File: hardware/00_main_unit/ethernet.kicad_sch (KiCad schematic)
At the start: 25 parts, among them IC5 LAN8742A, J11 LMJ1998824110DL1T39J, Y2 ABM7-25.000MHZ-D2Y-T

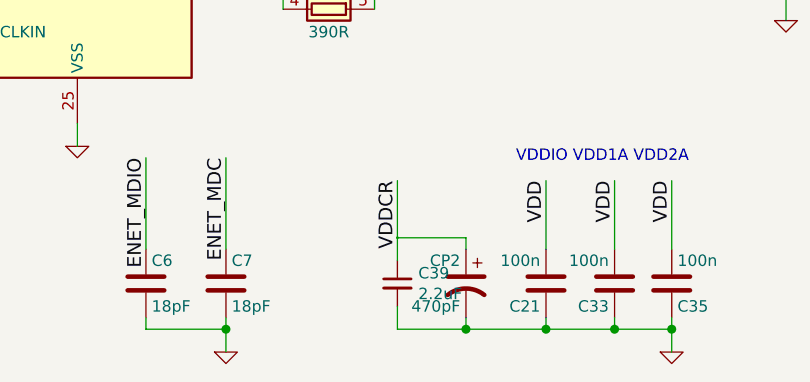
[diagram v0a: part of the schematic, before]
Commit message: Fixes after wrong merge
Signed-off-by: Jacek <matuszewski.kartech@gmail.com>
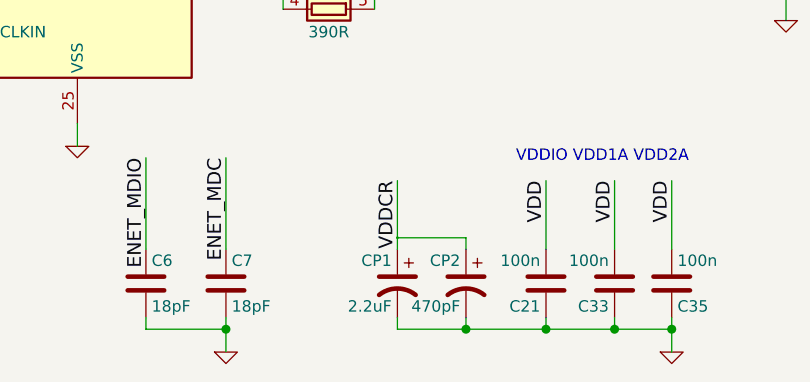
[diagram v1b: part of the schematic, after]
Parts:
- removed C39: 2.2uF, Capacitor_SMD:C_0603_1608Metric, symbol Device:C_Small
- added CP1: 2.2uF, Capacitor_SMD:C_0603_1608Metric, symbol Device:CP1
- C21, C33, C35, C36, C37: TME C0603C104K3RAC -> (none)
- C4, C5, C6, C7: TME 0603N180G500CT -> (none)
- C9: TME CL10A106MQ8NNNC -> (none)
- R1: TME WF06P-33R-5% -> (none)
- R38: TME SMD0603-12.1K-1% -> (none)
- R45, R46, R47, R48: TME SMD0603-49R9-1% -> (none)
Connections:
- net GND: now also CP1.2
- net VDDCR: now also CP1.1
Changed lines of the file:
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@@
     (stroke (width 0) (type solid) (color 0 0 0 0))
   )
-  (wire (pts (xy 168.91 129.54) (xy 168.91 132.08))
-    (stroke (width 0) (type solid) (color 0 0 0 0))
-  )
-  (wire (pts (xy 168.91 137.16) (xy 168.91 139.7))
+  (wire (pts (xy 168.91 129.54) (xy 168.91 130.81))
+    (stroke (width 0) (type solid) (color 0 0 0 0))
+  )
+  (wire (pts (xy 168.91 138.43) (xy 168.91 139.7))
     (stroke (width 0) (type solid) (color 0 0 0 0))
   )
@@
     )
     (property "Datasheet" "~" (id 3) (at 158.75 53.34 0)
-      (effects (font (size 1.27 1.27)) hide)
-    )
-    (property "TME" "CL10A106MQ8NNNC" (id 4) (at 158.75 53.34 0)
-      (effects (font (size 1.27 1.27)) hide)
-    )
-    (pin "1")
-    (pin "2")
-  )
-  (symbol (lib_id "Device:C_Small") (at 168.91 134.62 0) (unit 1)
-    (in_bom yes) (on_board yes)
-    (property "Reference" "C39" (id 0) (at 171.2342 133.4706 0)
-      (effects (font (size 1.27 1.27)) (justify left))
-    )
-    (property "Value" "2.2uF" (id 1) (at 171.2342 135.7693 0)
-      (effects (font (size 1.27 1.27)) (justify left))
-    )
-    (property "Footprint" "Capacitor_SMD:C_0603_1608Metric" (id 2) (at 168.91 134.62 0)
-      (effects (font (size 1.27 1.27)) hide)
-    )
-    (property "Datasheet" "~" (id 3) (at 168.91 134.62 0)
-      (effects (font (size 1.27 1.27)) hide)
-    )
-    (property "TME" "CL10A225KP8NNNC" (id 4) (at 168.91 134.62 0)
       (effects (font (size 1.27 1.27)) hide)
     )
@@
       (effects (font (size 0.762 0.762)))
     )
-    (property "TME" "WF06P-33R-5%" (id 4) (at 66.04 101.6 0)
-      (effects (font (size 1.27 1.27)) hide)
-    )
     (pin "1")
     (pin "2")
@@
       (effects (font (size 0.762 0.762)))
     )
-    (property "TME" "SMD0603-12.1K-1%" (id 4) (at 161.29 91.44 0)
-      (effects (font (size 1.27 1.27)) hide)
-    )
     (pin "1")
     (pin "2")
@@
       (effects (font (size 0.762 0.762)))
     )
-    (property "TME" "SMD0603-49R9-1%" (id 4) (at 166.37 68.58 0)
-      (effects (font (size 1.27 1.27)) hide)
-    )
     (pin "1")
     (pin "2")
@@
       (effects (font (size 0.762 0.762)))
     )
-    (property "TME" "SMD0603-49R9-1%" (id 4) (at 173.99 68.58 0)
-      (effects (font (size 1.27 1.27)) hide)
-    )
     (pin "1")
     (pin "2")
@@
       (effects (font (size 0.762 0.762)))
     )
-    (property "TME" "SMD0603-49R9-1%" (id 4) (at 181.61 68.58 0)
-      (effects (font (size 1.27 1.27)) hide)
-    )
     (pin "1")
     (pin "2")
@@
     (property "Datasheet" "~" (id 3) (at 189.23 68.58 0)
       (effects (font (size 0.762 0.762)))
-    )
-    (property "TME" "SMD0603-49R9-1%" (id 4) (at 189.23 68.58 0)
-      (effects (font (size 1.27 1.27)) hide)
     )
     (pin "1")
@@
       (effects (font (size 1.27 1.27)) hide)
     )
-    (property "TME" "0603N180G500CT" (id 4) (at 76.2 110.49 90)
+    (property "TME" "" (id 4) (at 76.2 110.49 90)
       (effects (font (size 1.27 1.27)) hide)
     )
@@
       (effects (font (size 1.27 1.27)) hide)
     )
-    (property "TME" "0603N180G500CT" (id 4) (at 76.2 121.92 90)
+    (property "TME" "" (id 4) (at 76.2 121.92 90)
       (effects (font (size 1.27 1.27)) hide)
     )
@@
       (effects (font (size 1.27 1.27)) hide)
     )
-    (property "TME" "0603N180G500CT" (id 4) (at 140.97 134.62 0)
-      (effects (font (size 1.27 1.27)) hide)
-    )
     (pin "1")
     (pin "2")
@@
       (effects (font (size 1.27 1.27)) hide)
     )
-    (property "TME" "0603N180G500CT" (id 4) (at 149.86 134.62 0)
+    (pin "1")
+    (pin "2")
+  )
+  (symbol (lib_id "Device:CP1") (at 168.91 134.62 0) (mirror y) (unit 1)
+    (in_bom yes) (on_board yes)
+    (property "Reference" "CP1" (id 0) (at 168.275 132.08 0)
+      (effects (font (size 1.27 1.27)) (justify left))
+    )
+    (property "Value" "2.2uF" (id 1) (at 168.275 137.16 0)
+      (effects (font (size 1.27 1.27)) (justify left))
+    )
+    (property "Footprint" "Capacitor_SMD:C_0603_1608Metric" (id 2) (at 168.91 134.62 0)
+      (effects (font (size 1.27 1.27)) hide)
+    )
+    (property "Datasheet" "" (id 3) (at 168.91 134.62 0)
       (effects (font (size 1.27 1.27)) hide)
     )
@@
       (effects (font (size 1.27 1.27)) hide)
     )
-    (property "TME" "C0603C104K3RAC" (id 4) (at 185.42 134.62 0)
-      (effects (font (size 1.27 1.27)) hide)
-    )
     (pin "1")
     (pin "2")
@@
       (effects (font (size 1.27 1.27)) hide)
     )
-    (property "TME" "C0603C104K3RAC" (id 4) (at 193.04 134.62 0)
-      (effects (font (size 1.27 1.27)) hide)
-    )
     (pin "1")
     (pin "2")
@@
       (effects (font (size 1.27 1.27)) hide)
     )
-    (property "TME" "C0603C104K3RAC" (id 4) (at 199.39 134.62 0)
-      (effects (font (size 1.27 1.27)) hide)
-    )
     (pin "1")
     (pin "2")
@@
       (effects (font (size 1.27 1.27)) hide)
     )
-    (property "TME" "C0603C104K3RAC" (id 4) (at 212.09 99.06 0)
-      (effects (font (size 1.27 1.27)) hide)
-    )
     (pin "1")
     (pin "2")
@@
       (effects (font (size 1.27 1.27)) hide)
     )
-    (property "TME" "C0603C104K3RAC" (id 4) (at 220.98 99.06 0)
-      (effects (font (size 1.27 1.27)) hide)
-    )

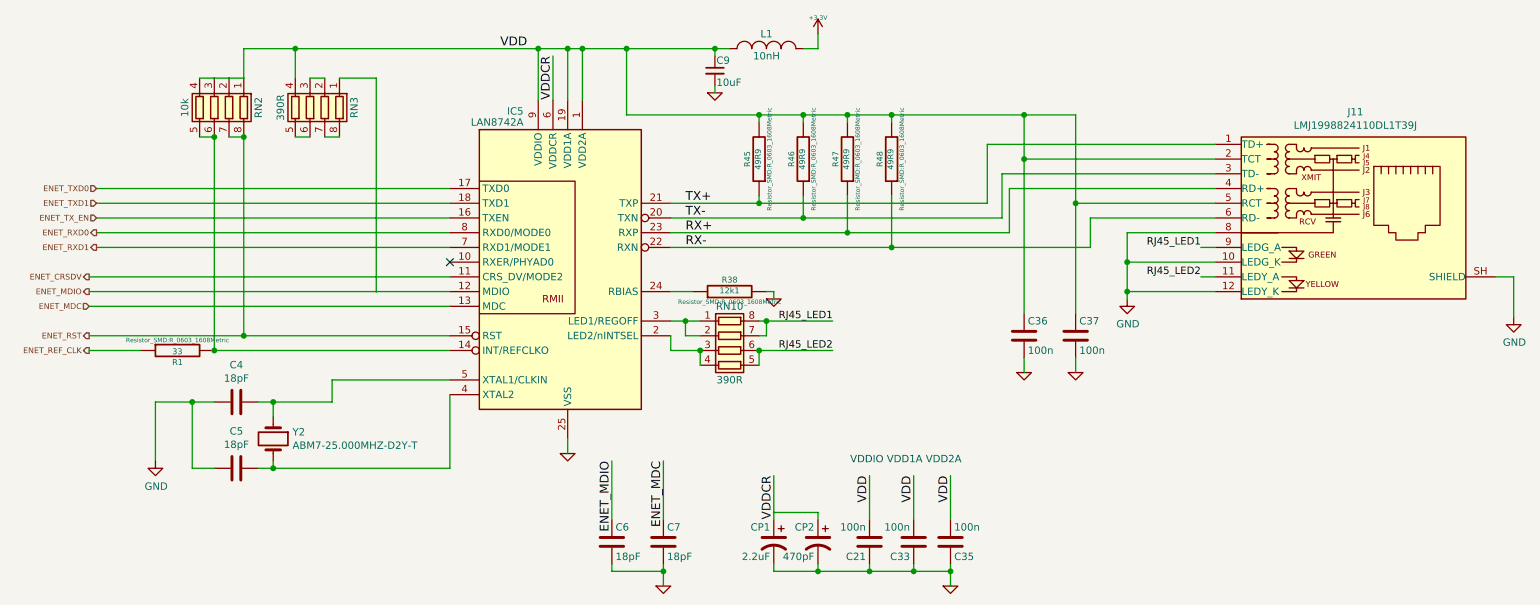
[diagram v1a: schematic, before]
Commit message: Remote mode fixes
Signed-off-by: Jarosław Karwik <jaroslaw.karwik@gmail.com>
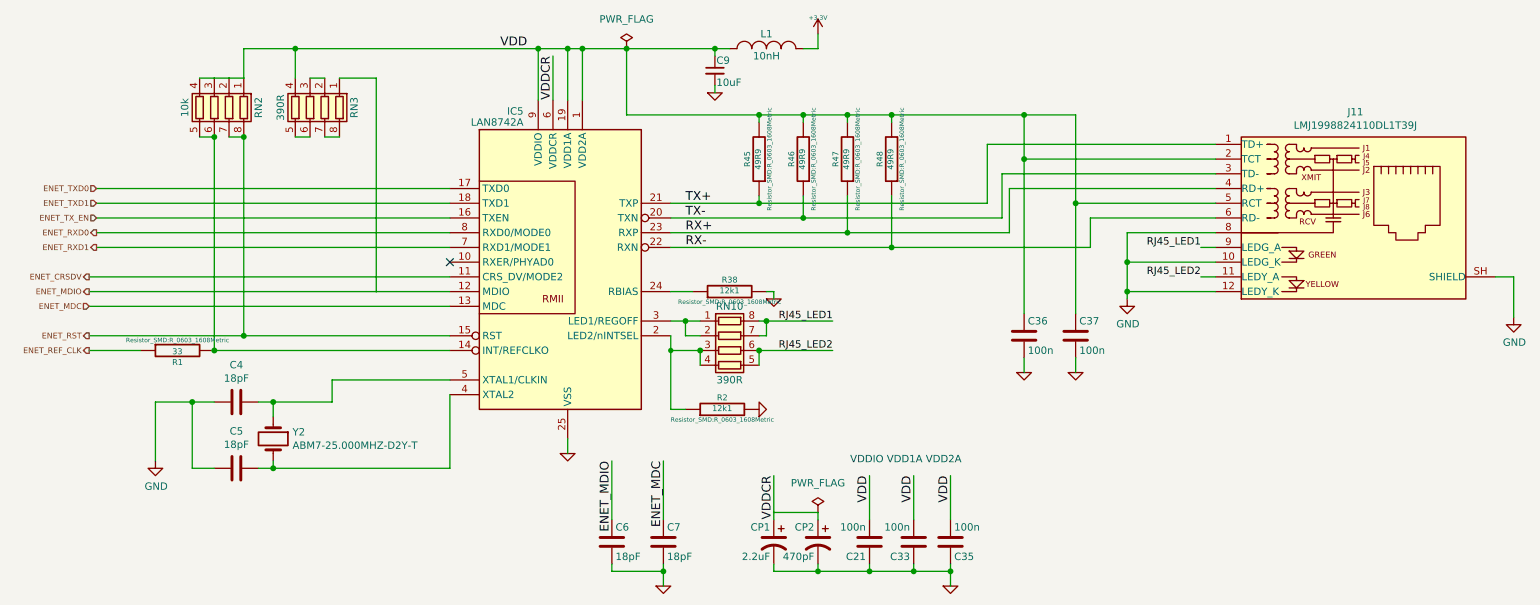
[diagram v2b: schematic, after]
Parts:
- added R2: 12k1, Resistor_SMD:R_0603_1608Metric, symbol step2cnc-rescue:R-RESCUE-step2cnc8_
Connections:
- net GND: now also R2.2
- net at IC5.2 (LED2/nINTSEL), RN10.3 (R3.1), RN10.4 (R4.1): now also R2.1
